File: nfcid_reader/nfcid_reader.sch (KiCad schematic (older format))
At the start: 20 parts, among them J1 BARREL_JACK, J2 ESP32_LEFT, J3 ESP32_RIGHT, J4 PN532, Q1 Q_PMOS_GSD, U1 MCP73832-2-OT, U2 LF33_TO220

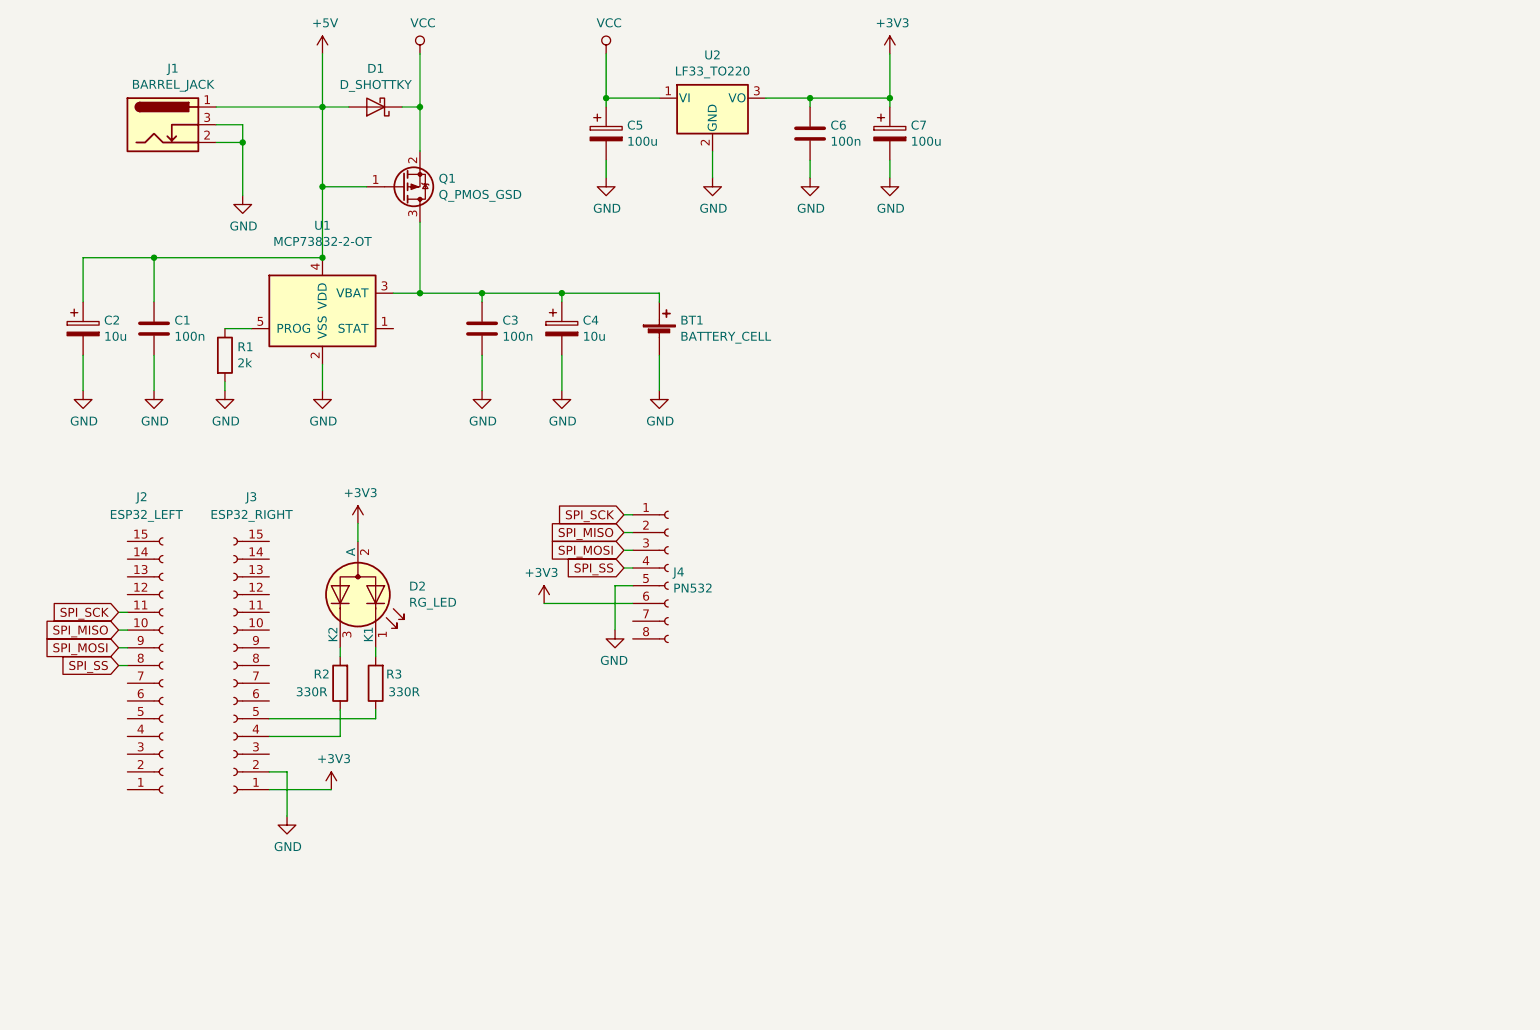
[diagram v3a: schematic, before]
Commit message: RC-1: Added votage dividers. J4 fliped.
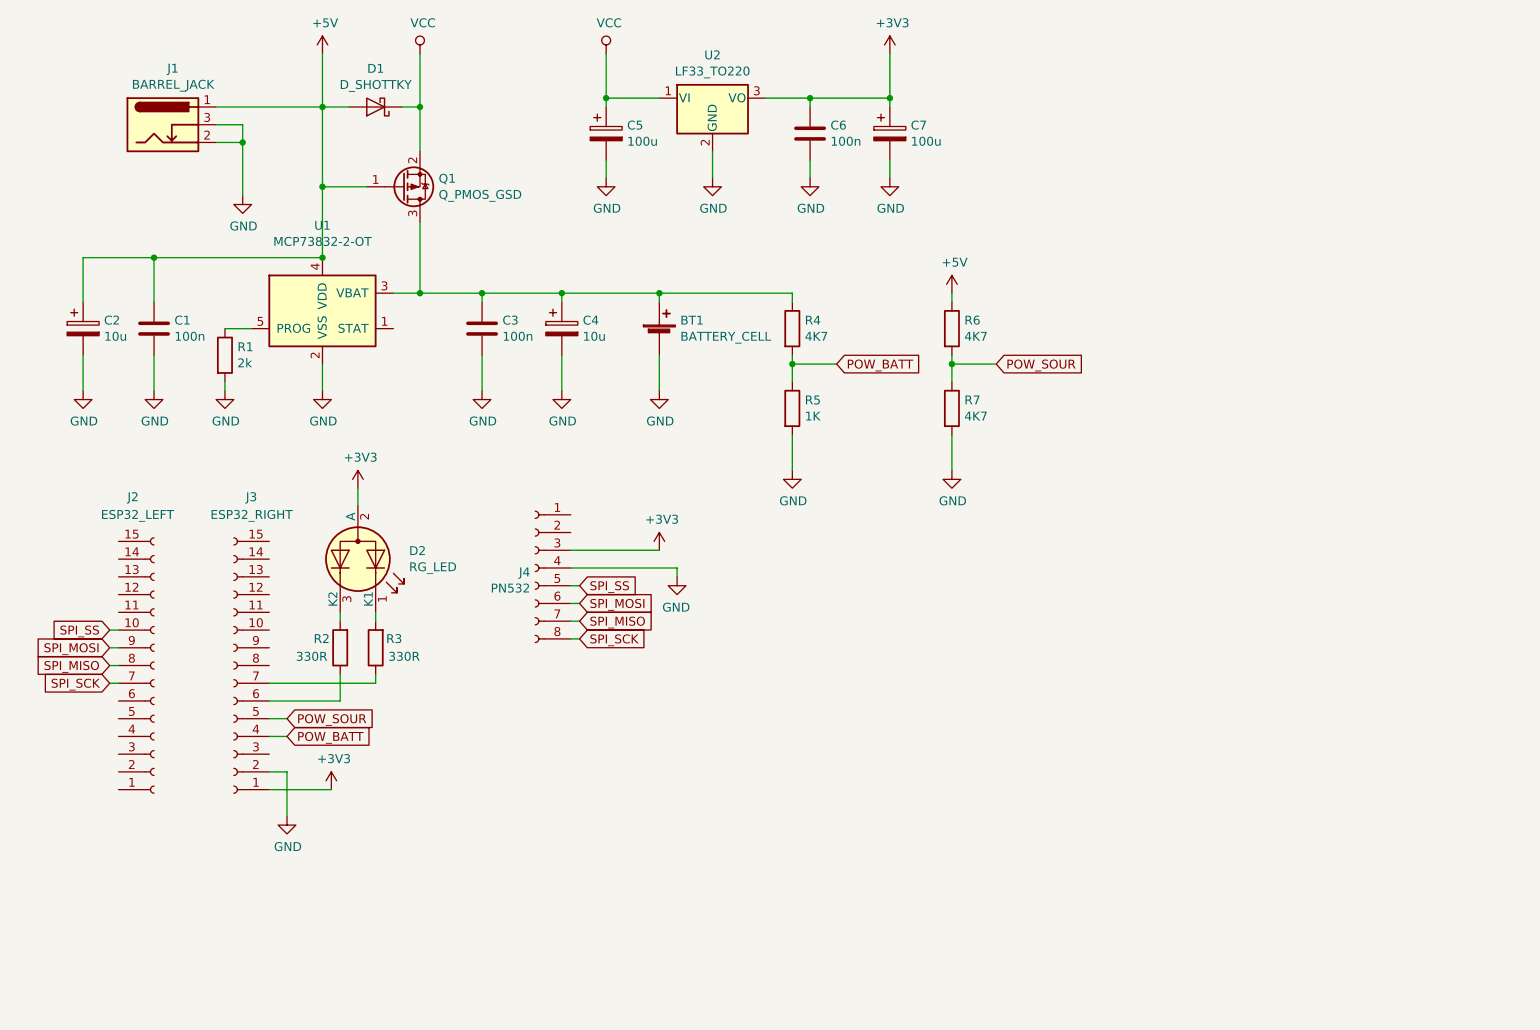
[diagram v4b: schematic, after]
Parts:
- added R4, R6, R7: 4K7, Resistor_THT:R_Axial_DIN0204_L3.6mm_D1.6mm_P7.62mm_Horizontal, symbol Device:R
- added R5: 1K, Resistor_THT:R_Axial_DIN0204_L3.6mm_D1.6mm_P7.62mm_Horizontal, symbol Device:R
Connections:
- net +3V3: now also J4.3 (Pin_3); no longer J4.6 (Pin_6)
- net +5V: now also R6.1
- net GND: now also J4.4 (Pin_4), R5.2, R7.2; no longer J4.5 (Pin_5)
- net SPI_MISO: now also J2.8 (Pin_8), J4.7 (Pin_7); no longer J2.10 (Pin_10), J4.2 (Pin_2)
- net SPI_MOSI: now also J4.6 (Pin_6); no longer J4.3 (Pin_3)
- net SPI_SCK: now also J2.7 (Pin_7), J4.8 (Pin_8); no longer J2.11 (Pin_11), J4.1 (Pin_1)
- net SPI_SS: now also J2.10 (Pin_10), J4.5 (Pin_5); no longer J2.8 (Pin_8), J4.4 (Pin_4)
- net at BT1.1 (+), C3.1, C4.1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: now also R4.1
- net at R2.1: now also J3.6 (Pin_6); no longer J3.4 (Pin_4)
- net at R3.1: now also J3.7 (Pin_7); no longer J3.5 (Pin_5)
- new net POW_BATT: J3.4 (Pin_4), R4.2, R5.1
- new net POW_SOUR: J3.5 (Pin_5), R6.2, R7.1
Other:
- moved on the sheet: D2, J2, J4, R2, R3

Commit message: RC-2: U2 changed to SMD. LED moved.
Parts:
- U2: footprint Package_TO_SOT_THT:TO-220-3_Vertical -> Package_TO_SOT_SMD:TO-252-2
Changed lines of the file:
@@
 F 0 "U2" H 4550 1342 50  0000 C CNN
 F 1 "LF33_TO220" H 4550 1251 50  0000 C CNN
-F 2 "Package_TO_SOT_THT:TO-220-3_Vertical" H 4550 1325 50  0001 C CIN
+F 2 "Package_TO_SOT_SMD:TO-252-2" H 4550 1325 50  0001 C CIN
 F 3 "http://www.st.com/content/ccc/resource/technical/document/datasheet/c4/0e/7e/2a/be/bc/4c/bd/CD00000546.pdf/files/CD00000546.pdf/jcr:content/translations/en.CD00000546.pdf" H 4550 1050 50  0001 C CNN
 	1    4550 1100

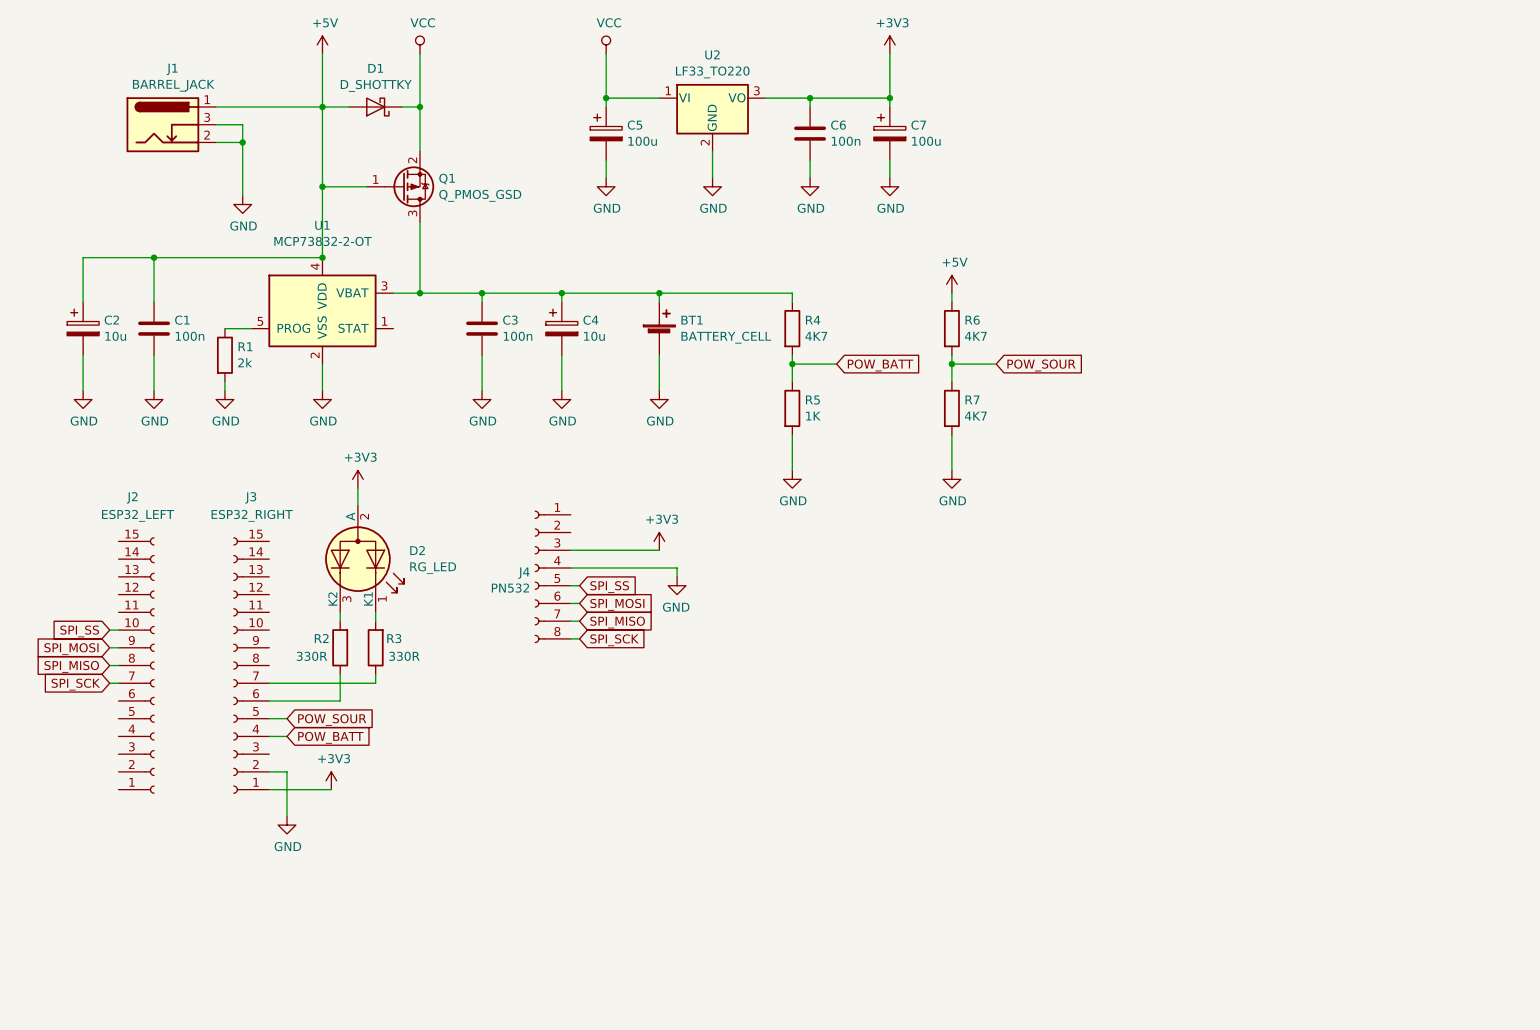
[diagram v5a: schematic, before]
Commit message: RC4: Fixed wrong ADC pin connection.
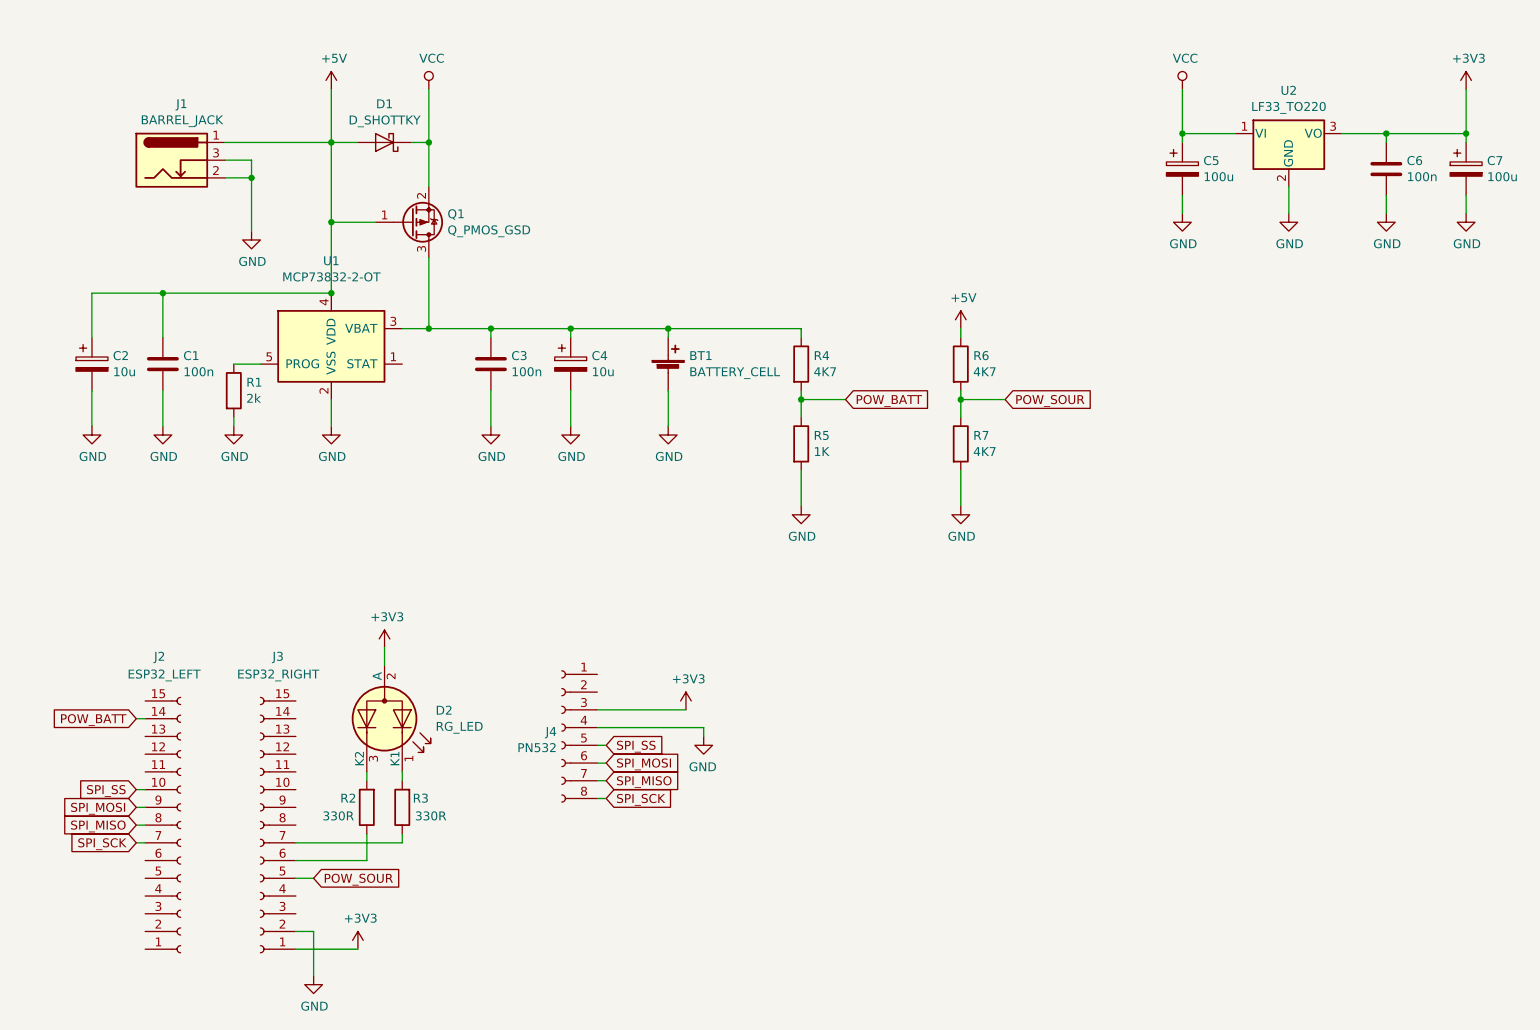
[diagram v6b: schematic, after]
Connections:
- net POW_BATT: now also J2.14 (Pin_14); no longer J3.4 (Pin_4)
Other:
- moved on the sheet: BT1, C1, C2, C3, C4, C5, C6, C7, D1, D2, J1, J2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
